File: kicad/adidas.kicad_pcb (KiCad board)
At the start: 2 copper layers, 152.7 x 107.2 mm, 24 parts

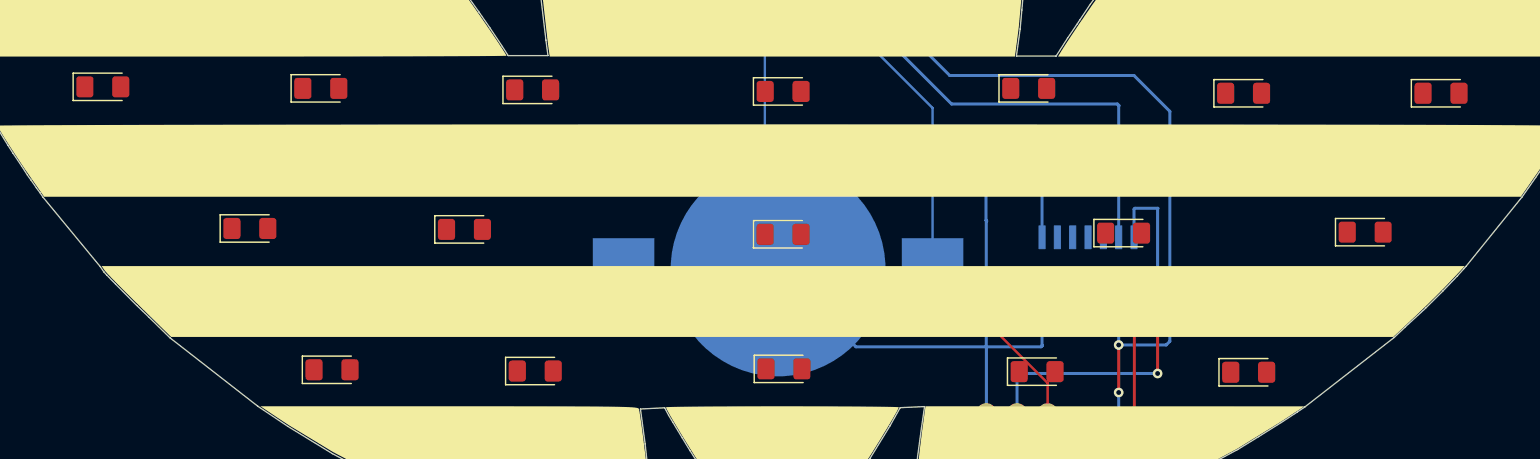
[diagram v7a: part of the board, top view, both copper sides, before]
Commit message: update schematic
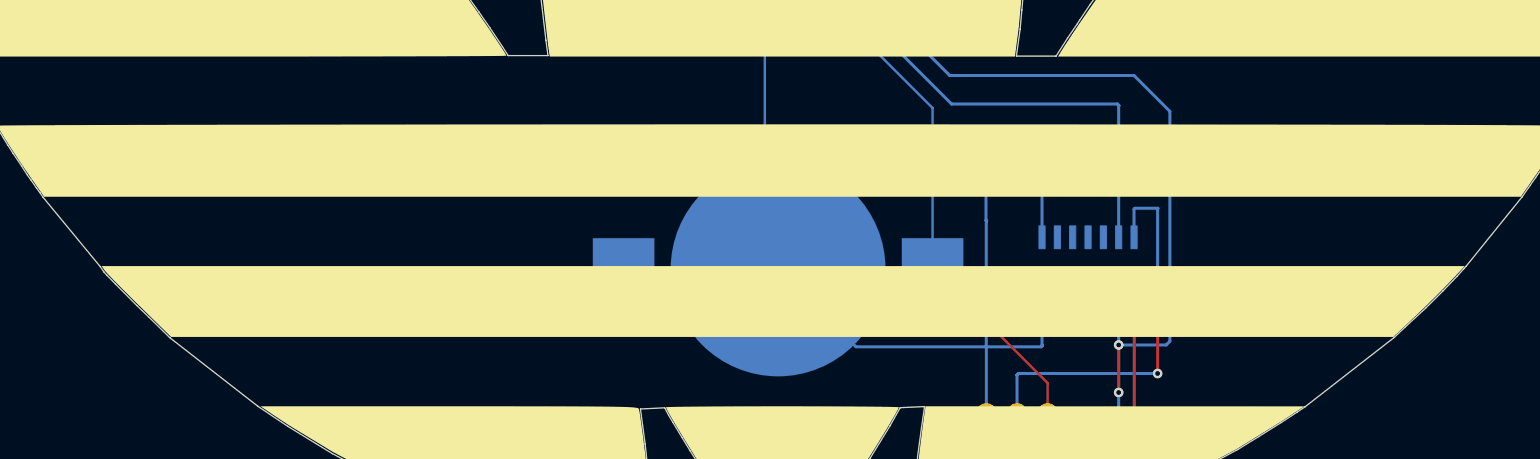
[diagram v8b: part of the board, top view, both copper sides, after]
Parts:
- removed the REF** at (213.4, 117.3)
- removed the REF** at (144.6, 128.9)
- removed the REF** at (219.7, 105.8)
- removed the REF** at (165.2, 117.5)
- removed the REF** at (193.4, 117.4)
- removed the REF** at (138.8, 117.1)
- removed the REF** at (121.0, 117.0)
- removed the REF** at (203.3, 105.8)
- removed the REF** at (144.4, 105.6)
- removed the REF** at (165.2, 105.7)
- removed the REF** at (203.7, 129.0)
- removed the REF** at (126.9, 105.4)
- removed the REF** at (108.8, 105.3)
- removed the REF** at (186.2, 128.9)
- removed the REF** at (165.2, 128.7)
- removed the REF** at (185.5, 105.4)
- removed the REF** at (127.8, 128.8)
